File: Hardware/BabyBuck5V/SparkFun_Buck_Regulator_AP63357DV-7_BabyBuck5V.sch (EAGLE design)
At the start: 20 parts, among them U1 AP63357

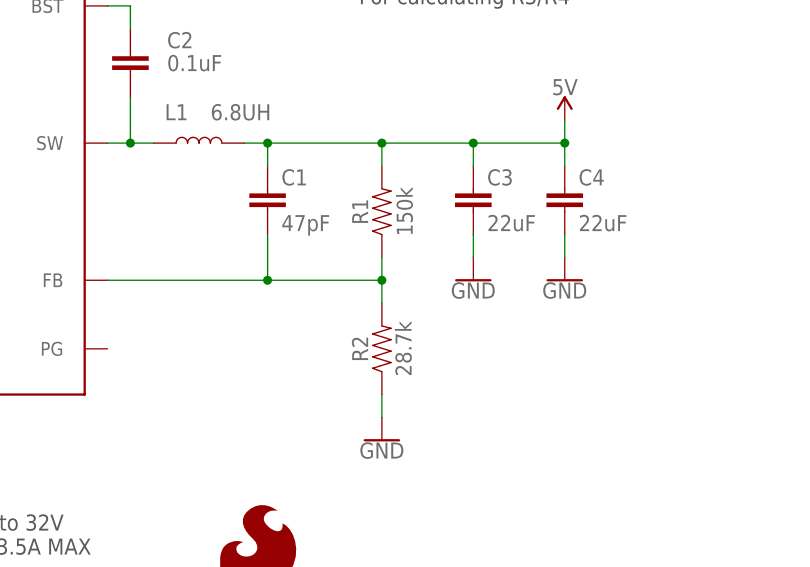
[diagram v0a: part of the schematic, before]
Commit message: Prepare for v10 reds order.
Change R1/R2 to better match 5V output requirement.
Repanelize.
Reorganize Production Folder Structure.
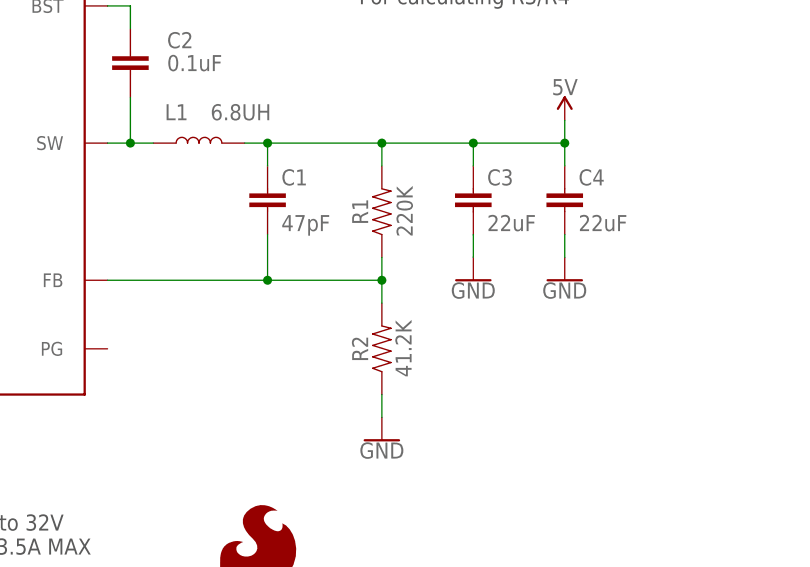
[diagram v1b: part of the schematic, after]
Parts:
- R1: value 150k -> 220K; device SparkFun-Resistors:150KOHM-0402T-1/16W-1% -> SparkFun-Resistors:220KOHM-0402T-1/16W-1%; RES 150k -> 220K
- R2: value 28.7k -> 41.2K; device Buck5V:28.7KOHM-0402-1/16W-1%(28.7KOHM) -> Buck5V:41.2KOHM-0402-1/16W-1%(41.2KOHM)
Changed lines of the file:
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@@
 <part name="FD2" library="SparkFun-Aesthetics" deviceset="FIDUCIAL" device="UFIDUCIAL"/>
 <part name="FD4" library="SparkFun-Aesthetics" deviceset="FIDUCIAL" device="UFIDUCIAL"/>
-<part name="R2" library="Buck5V" deviceset="28.7KOHM" device="-0402-1/16W-1%(28.7KOHM)" value="28.7k"/>
+<part name="R2" library="Buck5V" deviceset="41.2KOHM" device="-0402-1/16W-1%(41.2KOHM)" value="41.2K"/>
 <part name="U1" library="Buck5V" deviceset="AP63357" device="" value="AP63357"/>
-<part name="R1" library="SparkFun-Resistors" deviceset="150KOHM" device="-0402T-1/16W-1%" value="150k">
-<attribute name="RES" value="150k"/>
+<part name="R1" library="SparkFun-Resistors" deviceset="220KOHM" device="-0402T-1/16W-1%" value="220K">
+<attribute name="RES" value="220K"/>
 </part>
 <part name="C1" library="SparkFun-Capacitors" deviceset="47PF" device="-0402_TIGHT-25V-5%-X7R" value="47pF"/>
